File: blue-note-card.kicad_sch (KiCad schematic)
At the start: 27 parts, among them J15 N_GR1, J3 MDT420E01001, J7 SF72S006VBAR2500, J9 N_GR2

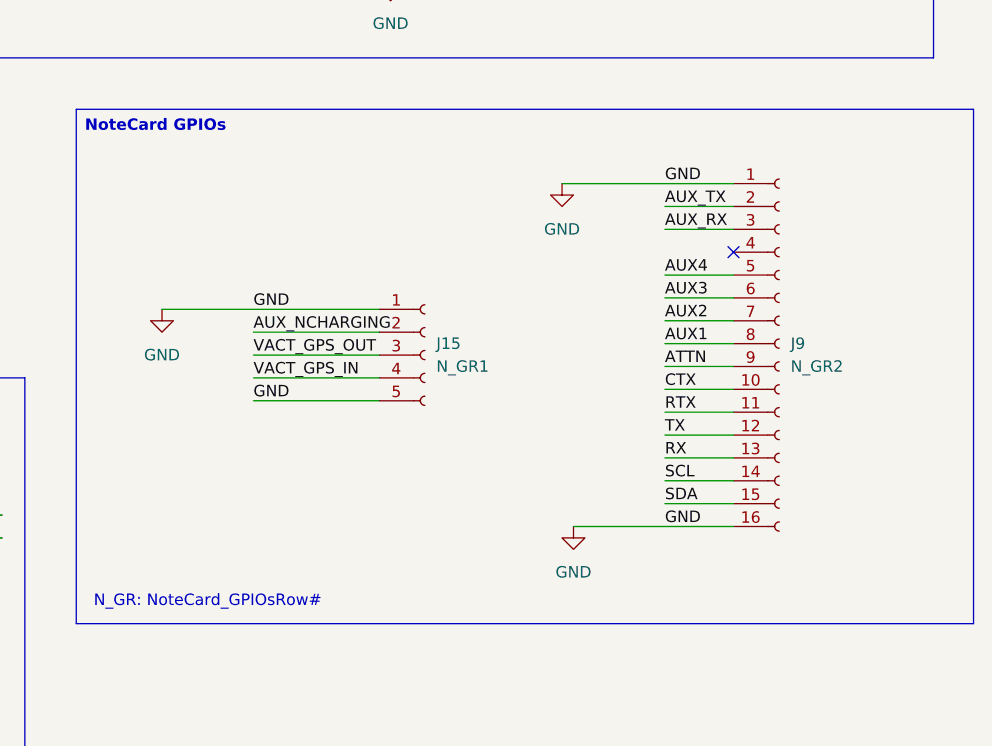
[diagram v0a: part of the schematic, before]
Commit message: Layout parts
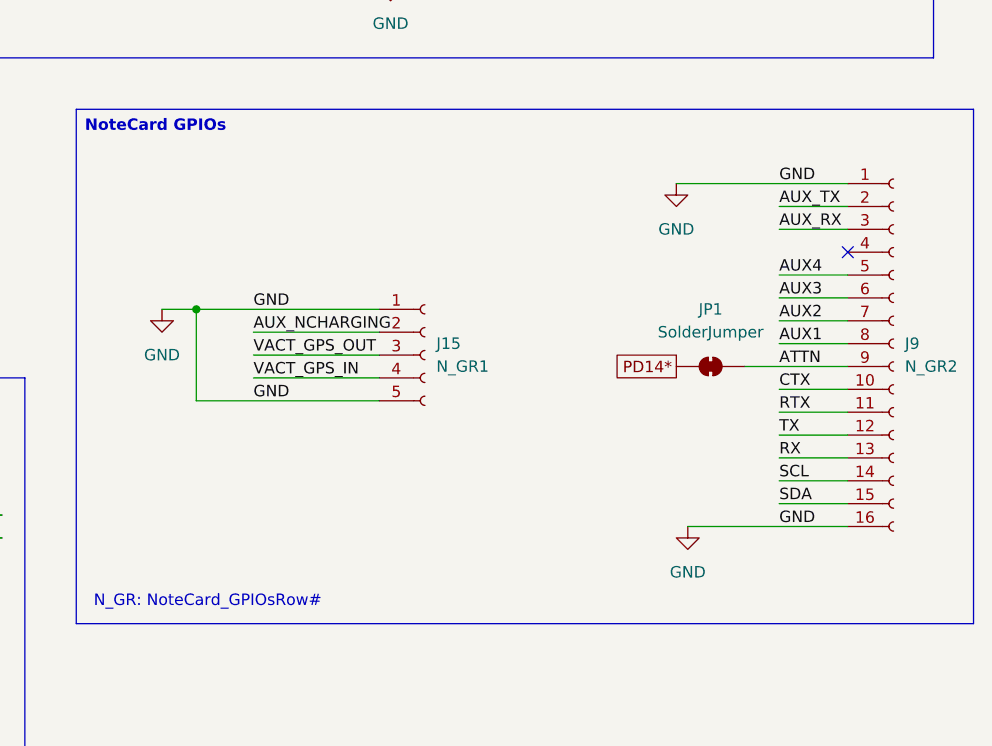
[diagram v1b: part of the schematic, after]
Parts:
- added JP1: SolderJumper, Jumper:SolderJumper-2_P1.3mm_Bridged_RoundedPad1.0x1.5mm, symbol Jumper:SolderJumper_2_Bridged
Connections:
- net ATTN: now also JP1.2 (B)
- new net PD14*: JP1.1 (A)
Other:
- moved on the sheet: J9

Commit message: Layout
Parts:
- removed JP1: SolderJumper, Jumper:SolderJumper-2_P1.3mm_Bridged_RoundedPad1.0x1.5mm, symbol Jumper:SolderJumper_2_Bridged
- added JP1: SolderJumper_2_Open, Jumper:SolderJumper-2_P1.3mm_Open_RoundedPad1.0x1.5mm, symbol Jumper:SolderJumper_2_Open
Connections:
- net +3.3V Buck: now also J3.2, J3.4
- net ATTN: now also J9.6 (Pin_6); no longer J9.9 (Pin_9)
- net AUX1: now also J9.10 (Pin_10); no longer J9.8 (Pin_8)
- net AUX2: now also J9.9 (Pin_9); no longer J9.7 (Pin_7)
- net AUX3: now also J9.8 (Pin_8); no longer J9.6 (Pin_6)
- net AUX4: now also J9.7 (Pin_7); no longer J9.5 (Pin_5)
- net AUX_NCHARGING: now also J9.13 (Pin_13); no longer J15.2 (Pin_2)
- net AUX_RX: now also J9.5 (Pin_5); no longer J9.3 (Pin_3)
- net AUX_TX: now also J9.4 (Pin_4); no longer J9.2 (Pin_2)
- net CTX: now also J15.2 (Pin_2); no longer J9.10 (Pin_10)
- net GND: no longer J3.2, J3.4
- net RTX: now also J15.3 (Pin_3); no longer J9.11 (Pin_11)
- net RX: now also J9.3 (Pin_3); no longer J9.13 (Pin_13)
- net SCL: now also J9.12 (Pin_12); no longer J9.14 (Pin_14)
- net SDA: now also J9.11 (Pin_11); no longer J9.15 (Pin_15)
- net TX: now also J9.2 (Pin_2); no longer J9.12 (Pin_12)
- net VACT_GPS_IN: now also J9.14 (Pin_14), JP1.1 (A); no longer J15.4 (Pin_4)
- net VACT_GPS_OUT: now also J9.15 (Pin_15), JP1.2 (B); no longer J15.3 (Pin_3)

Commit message: Fixed DRC errors
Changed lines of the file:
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@@
-	(wire
-		(pts
-			(xy 259.08 116.84) (xy 266.7 116.84)
-		)
-		(stroke
-			(width 0)
-			(type default)
-		)
-	)
 	(wire
 		(pts

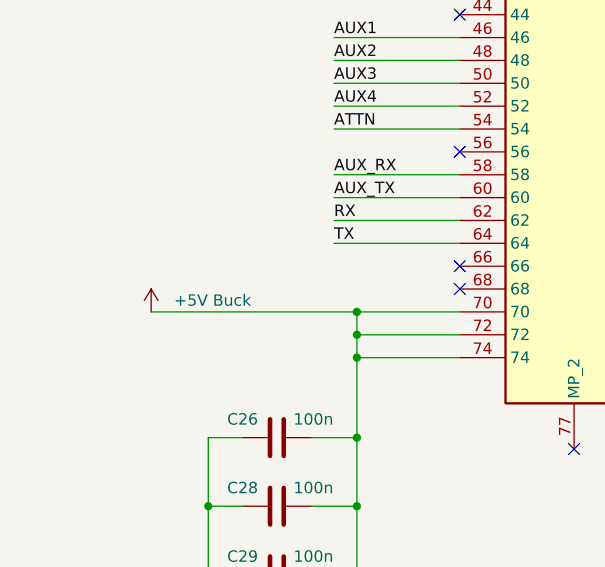
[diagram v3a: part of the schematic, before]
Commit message: Added ORing VBUS
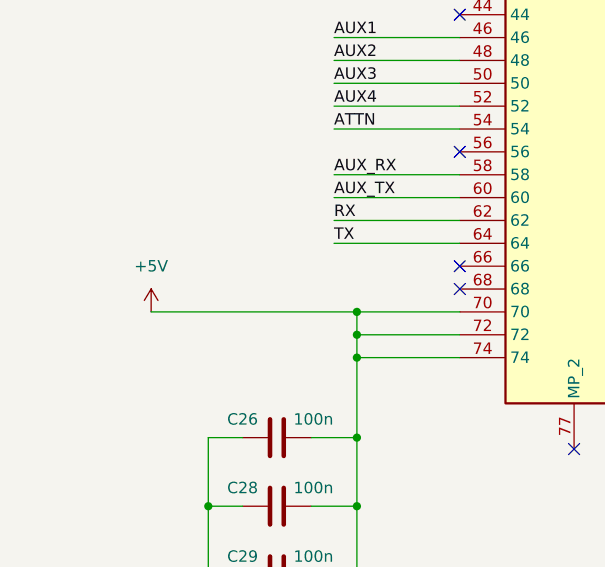
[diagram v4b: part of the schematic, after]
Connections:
- net +5V Buck renamed +5V
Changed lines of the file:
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@@
 			)
 		)
-		(property "Value" "+5V Buck"
-			(at 22.86 121.9199 0)
+		(property "Value" "+5V"
+			(at 20.32 118.11 0)
 			(effects
 				(font
 					(size 1.27 1.27)
 				)
-				(justify left)
 			)
 		)

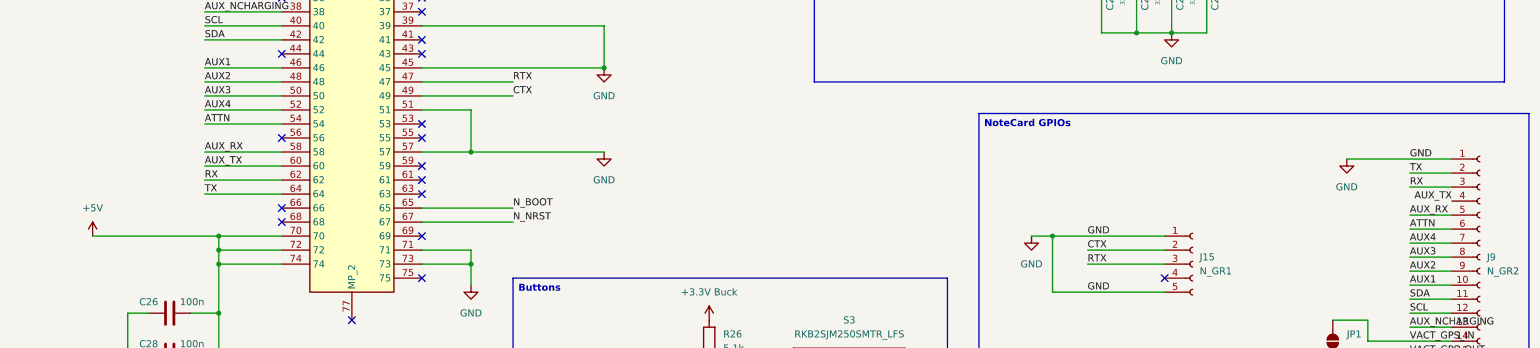
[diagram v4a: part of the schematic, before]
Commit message: Added LED indicators, USER LEDs, extended layout, fixed footprints
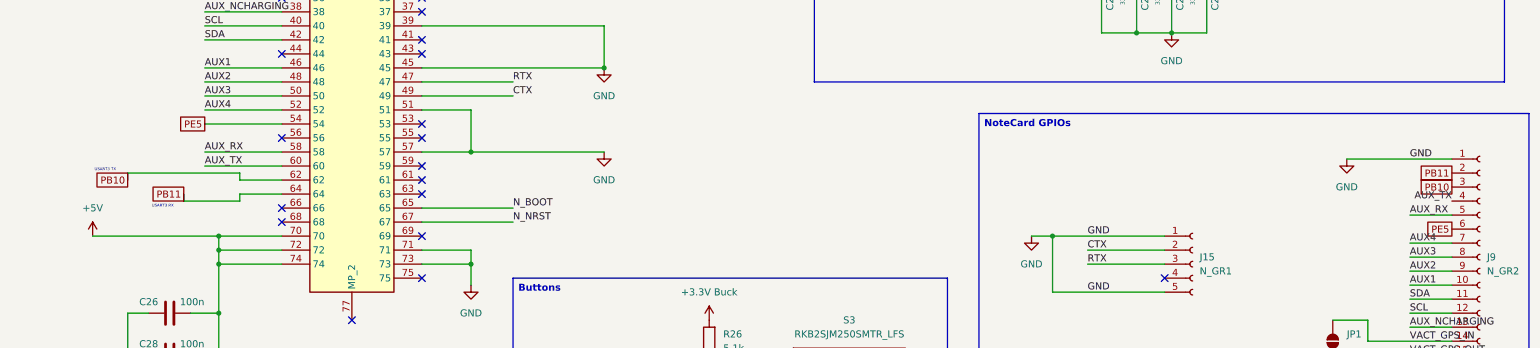
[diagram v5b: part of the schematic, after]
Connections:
- net ATTN renamed PE5
- net RX renamed PB10
- net TX renamed PB11
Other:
- note added: "USART3 RX"
- note added: "USART3 TX"
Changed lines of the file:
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@@
+		)
+	)
+	(text "USART3 RX"
+		(exclude_from_sim no)
+		(at 33.02 117.856 0)
+		(effects
+			(font
+				(size 0.508 0.508)
+			)
+		)
+	)
+	(text "USART3 TX"
+		(exclude_from_sim no)
+		(at 22.606 111.252 0)
+		(effects
+			(font
+				(size 0.508 0.508)
+			)
 		)
 	)
@@
 	(wire
 		(pts
+			(xy 46.99 115.57) (xy 46.99 116.84)
+		)
+		(stroke
+			(width 0)
+			(type default)
+		)
+	)
+	(wire
+		(pts
 			(xy 264.16 33.02) (xy 264.16 35.56)
 		)
@@
 	(wire
 		(pts
+			(xy 46.99 111.76) (xy 26.67 111.76)
+		)
+		(stroke
+			(width 0)
+			(type default)
+		)
+	)
+	(wire
+		(pts
 			(xy 30.48 137.16) (xy 26.67 137.16)
 		)
@@
 	(wire
 		(pts
+			(xy 36.83 116.84) (xy 36.83 115.57)
+		)
+		(stroke
+			(width 0)
+			(type default)
+		)
+	)
+	(wire
+		(pts
 			(xy 19.05 67.31) (xy 54.61 67.31)
 		)
@@
 	(wire
 		(pts
-			(xy 259.08 111.76) (xy 266.7 111.76)
-		)
-		(stroke
-			(width 0)
-			(type default)
-		)
-	)
-	(wire
-		(pts
 			(xy 167.64 66.04) (xy 160.02 66.04)
 		)
@@
 	(wire
 		(pts
-			(xy 54.61 115.57) (xy 40.64 115.57)
+			(xy 54.61 115.57) (xy 46.99 115.57)
 		)
 		(stroke
@@
 	(wire
 		(pts
+			(xy 46.99 113.03) (xy 46.99 111.76)
+		)
+		(stroke
+			(width 0)
+			(type default)
+		)
+	)
+	(wire
+		(pts
 			(xy 80.01 107.95) (xy 88.9 107.95)
 		)
@@
 	(wire
 		(pts
-			(xy 259.08 114.3) (xy 266.7 114.3)
-		)
-		(stroke
-			(width 0)
-			(type default)
-		)
-	)
-	(wire
-		(pts
 			(xy 264.16 40.64) (xy 264.16 43.18)
 		)
@@
 	(wire
 		(pts
+			(xy 26.67 111.76) (xy 26.67 113.03)
+		)
+		(stroke
+			(width 0)
+			(type default)
+		)
+	)
+	(wire
+		(pts
 			(xy 80.01 97.79) (xy 96.52 97.79)
 		)
@@
 	(wire
 		(pts
-			(xy 259.08 121.92) (xy 266.7 121.92)
-		)
-		(stroke
-			(width 0)
-			(type default)
-		)
-	)
-	(wire
-		(pts
 			(xy 196.85 45.72) (xy 209.55 45.72)
 		)
@@
 	(wire
 		(pts
-			(xy 54.61 113.03) (xy 40.64 113.03)
+			(xy 54.61 113.03) (xy 46.99 113.03)
 		)
 		(stroke
@@
 		(pts
 			(xy 251.46 144.78) (xy 266.7 144.78)
+		)
+		(stroke
+			(width 0)
+			(type default)
+		)
+	)
+	(wire
+		(pts
+			(xy 46.99 116.84) (xy 36.83 116.84)
 		)
 		(stroke
@@
 		)
 	)
-	(label "TX"
-		(at 259.08 111.76 0)
-		(effects
-			(font
-				(size 1.27 1.27)
-				(thickness 0.1588)
-			)
-			(justify left bottom)
-		)
-	)
 	(label "GND"
 		(at 200.66 123.19 0)
@@
 		)
 	)
-	(label "RX"
-		(at 40.64 113.03 0)
-		(effects
-			(font
-				(size 1.27 1.27)
-			)
-			(justify left bottom)
-		)
-	)
 	(label "RTX"
 		(at 96.52 95.25 0)
@@
 		)
 	)
-	(label "TX"
-		(at 40.64 115.57 0)
-		(effects
-			(font
-				(size 1.27 1.27)
-			)
-			(justify left bottom)
-		)
-	)
 	(label "SCL"
 		(at 259.08 137.16 0)
@@
 		)
 	)
-	(label "RX"
-		(at 259.08 114.3 0)
-		(effects
-			(font
-				(size 1.27 1.27)
-				(thickness 0.1588)
-			)
-			(justify left bottom)
-		)
-	)
-	(label "ATTN"
-		(at 40.64 102.87 0)
-		(effects
-			(font
-				(size 1.27 1.27)
-			)
-			(justify left bottom)
-		)
-	)
 	(label "SIM_RST"
 		(at 173.99 35.56 0)
@@
 		)
 	)
-	(label "ATTN"
-		(at 259.08 121.92 0)
-		(effects
-			(font
-				(size 1.27 1.27)
-			)
-			(justify left bottom)
-		)
-	)
 	(label "SIM_RST"
 		(at 40.64 57.15 0)
@@
 		)
 	)
+	(global_label "PE5"
+		(shape passive)
+		(at 266.7 121.92 180)
+		(fields_autoplaced yes)
+		(effects
+			(font
+				(size 1.27 1.27)
+			)
+			(justify right)
+		)
+		(property "Intersheetrefs" "${INTERSHEET_REFS}"
+			(at 261.1976 121.92 0)
+			(effects
+				(font
+					(size 1.27 1.27)
+				)
+				(justify right)
+				(hide yes)
+			)
+		)
+	)
+	(global_label "PB11"
+		(shape passive)
+		(at 36.83 115.57 180)
+		(fields_autoplaced yes)
+		(effects
+			(font
+				(size 1.27 1.27)
+			)
+			(justify right)
+		)
+		(property "Intersheetrefs" "${INTERSHEET_REFS}"
+			(at 29.9971 115.57 0)
+			(effects
+				(font
+					(size 1.27 1.27)
+				)
+				(justify right)
+				(hide yes)
+			)
+		)
+	)
+	(global_label "PB10"
+		(shape passive)
+		(at 26.67 113.03 180)
+		(fields_autoplaced yes)
+		(effects
+			(font
+				(size 1.27 1.27)
+			)
+			(justify right)
+		)
+		(property "Intersheetrefs" "${INTERSHEET_REFS}"
+			(at 19.8371 113.03 0)
+			(effects
+				(font
+					(size 1.27 1.27)
+				)
+				(justify right)
+				(hide yes)
+			)
+		)
+	)
+	(global_label "PE5"
+		(shape passive)
+		(at 40.64 102.87 180)
+		(fields_autoplaced yes)
+		(effects
+			(font
+				(size 1.27 1.27)
+			)
+			(justify right)
+		)
+		(property "Intersheetrefs" "${INTERSHEET_REFS}"
+			(at 35.1376 102.87 0)
+			(effects
+				(font
+					(size 1.27 1.27)
+				)
+				(justify right)
+				(hide yes)
+			)
+		)
+	)
+	(global_label "PB11"
+		(shape passive)
+		(at 266.7 111.76 180)
+		(fields_autoplaced yes)
+		(effects
+			(font
+				(size 1.27 1.27)
+			)
+			(justify right)
+		)
+		(property "Intersheetrefs" "${INTERSHEET_REFS}"
+			(at 259.8671 111.76 0)
+			(effects
+				(font
+					(size 1.27 1.27)
+				)
+				(justify right)
+				(hide yes)
+			)
+		)
+	)
+	(global_label "PB10"
+		(shape passive)
+		(at 266.7 114.3 180)
+		(fields_autoplaced yes)
+		(effects
+			(font
+				(size 1.27 1.27)
+			)
+			(justify right)
+		)
+		(property "Intersheetrefs" "${INTERSHEET_REFS}"
+			(at 259.8671 114.3 0)
+			(effects
+				(font
+					(size 1.27 1.27)
+				)
+				(justify right)
+				(hide yes)
+			)
+		)
+	)

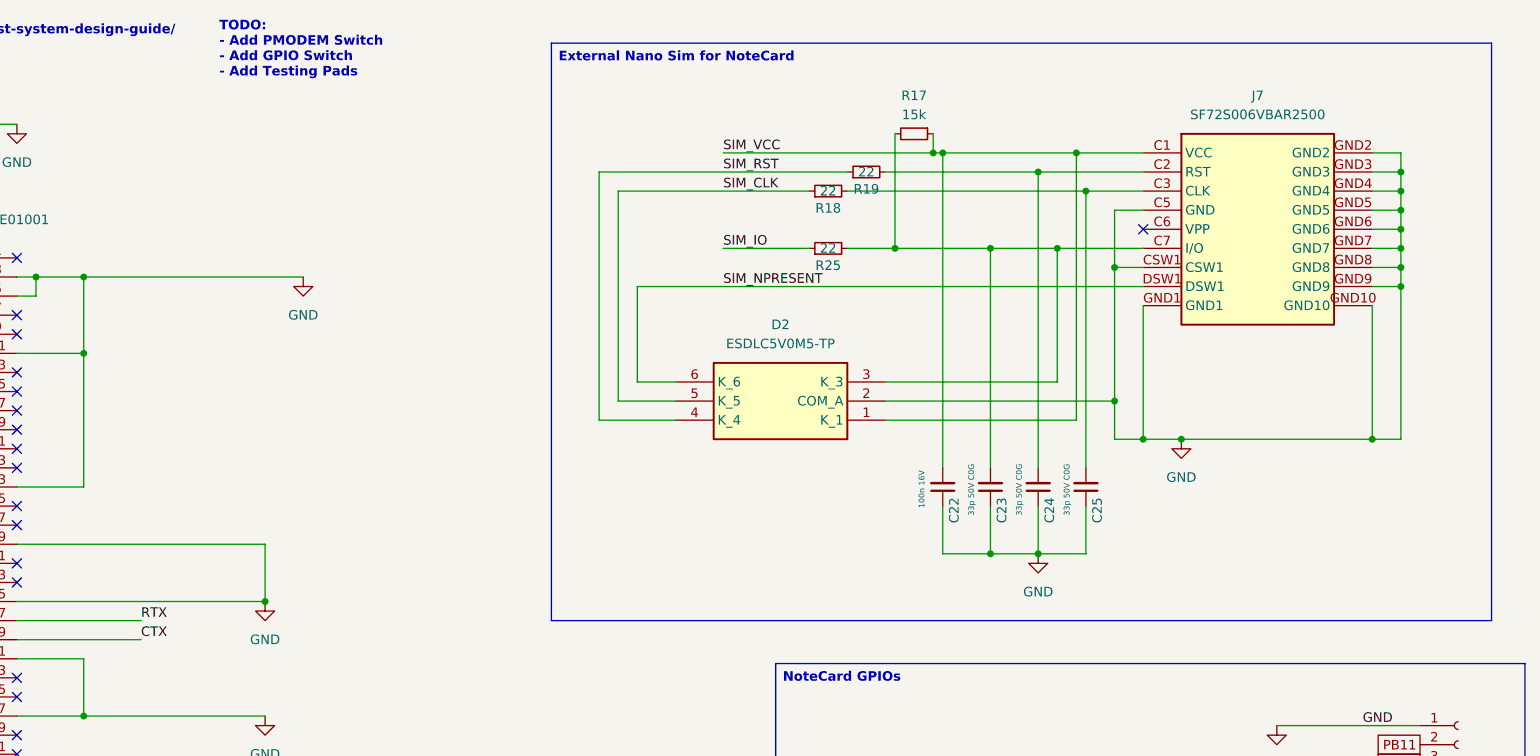
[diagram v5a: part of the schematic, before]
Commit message: Relayout NanoSim component
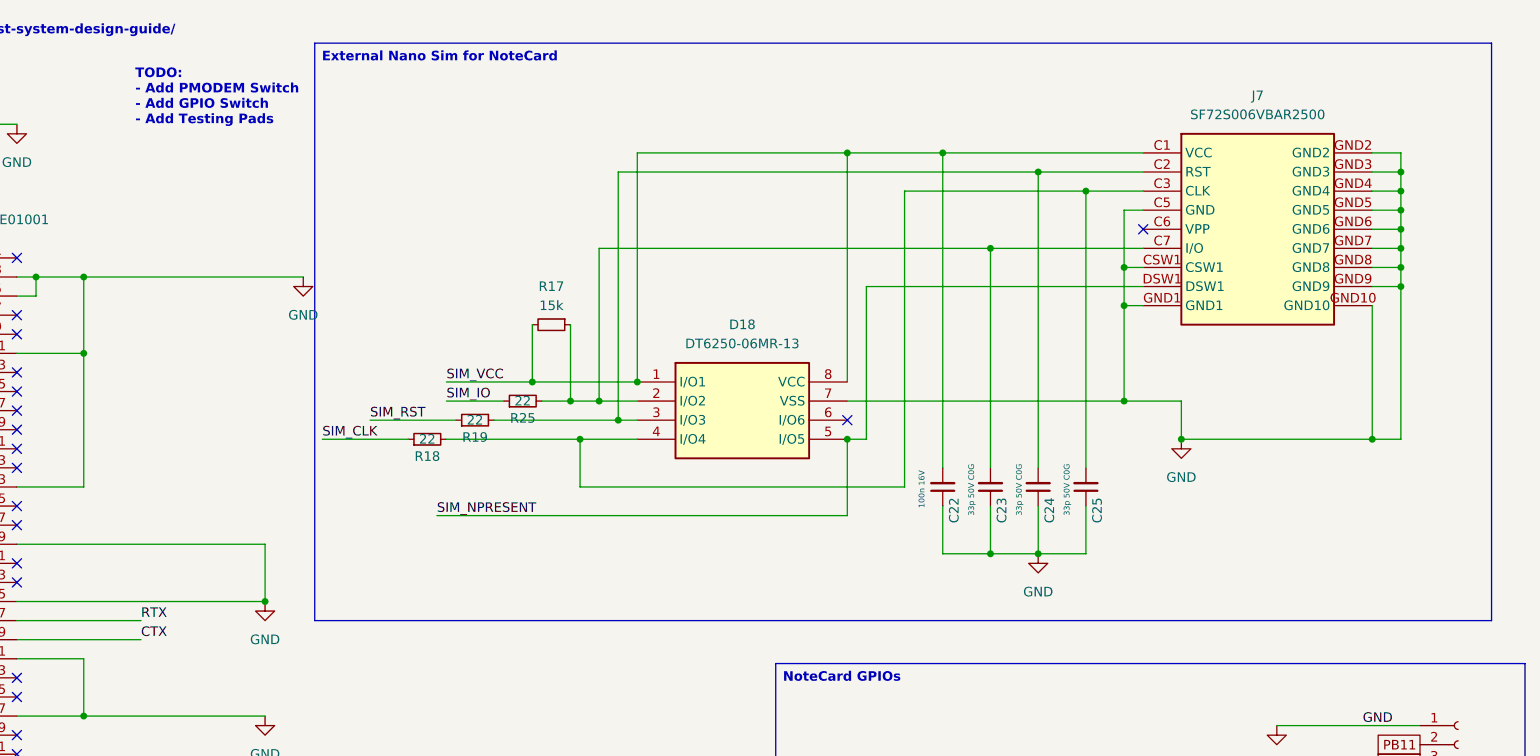
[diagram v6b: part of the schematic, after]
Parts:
- removed D2: ESDLC5V0M5-TP, SamacSys_Parts:SOTFL50P160X60-6N, symbol SamacSys_Parts:ESDLC5V0M5-TP
- added D18: DT6250-06MR-13, SamacSys_Parts:SOP65P490X110-8N, symbol SamacSys_Parts:DT6250-06MR-13
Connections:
- net GND: now also D18.7 (VSS)
- net SIM_NPRESENT: now also D18.5 (I/O5)
- net SIM_VCC: now also R17.2, D18.1 (I/O1), D18.8 (VCC); no longer R17.1
- net at C25.2, J7.C3 (CLK), R18.2: now also D18.4 (I/O4)
- net at C23.2, J7.C7 (I/O), R25.2: now also R17.1, D18.2 (I/O2); no longer R17.2
- net at C24.2, J7.C2 (RST), R19.2: now also D18.3 (I/O3)
- no-connect marks 31 -> 32
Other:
- moved on the sheet: R17, R18, R19, R25

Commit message: Added changes
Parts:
- removed J15: N_GR1, Connector_PinSocket_2.00mm:PinSocket_1x05_P2.00mm_Vertical, symbol Connector:Conn_01x05_Socket
- removed J9: N_GR2, Connector_PinSocket_2.00mm:PinSocket_1x16_P2.00mm_Vertical, symbol Connector:Conn_01x16_Socket
- added J17: N_GR1, Connector_PinSocket_2.00mm:PinSocket_1x20_P2.00mm_Vertical, symbol Connector:Conn_01x20_Socket
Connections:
- net AUX1: now also J17.10 (Pin_10)
- net AUX2: now also J17.9 (Pin_9)
- net AUX3: now also J17.8 (Pin_8)
- net AUX4: now also J17.7 (Pin_7)
- net AUX_NCHARGING: now also J17.13 (Pin_13)
- net AUX_RX: now also J17.5 (Pin_5)
- net AUX_TX: now also J17.4 (Pin_4)
- net CTX: now also J17.16 (Pin_16)
- net GND: now also J17.1 (Pin_1), J17.18 (Pin_18), J17.19 (Pin_19), J17.20 (Pin_20)
- net PB10: now also J17.3 (Pin_3)
- net PB11: now also J17.2 (Pin_2)
- net PE5: now also J17.6 (Pin_6)
- net RTX: now also J17.17 (Pin_17)
- net SCL: now also J17.12 (Pin_12)
- net SDA: now also J17.11 (Pin_11)
- net VACT_GPS_IN: now also J17.14 (Pin_14)
- net VACT_GPS_OUT: now also J17.15 (Pin_15)
- no-connect marks 32 -> 31

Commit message: Fixed things
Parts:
- removed C54, C55: 100n, Capacitor_SMD:C_0603_1608Metric_Pad1.08x0.95mm_HandSolder, symbol Device:C
- removed R26, R27: 5.1k, Resistor_SMD:R_0603_1608Metric_Pad0.98x0.95mm_HandSolder, symbol Device:R
- removed S4: RKB2SJM250SMTR_LFS, SamacSys_Parts:RKB2SJM250SMTRLFS, symbol SamacSys_Parts:RKB2SJM250SMTR_LFS
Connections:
- net +3.3V Buck renamed +3.3V NOTE
- net +5V renamed +5V NOTE
- net N_BOOT: no longer names the net of J3.65
- net PB10 renamed PB10_PIN_HEADER
- no-connect marks 31 -> 32
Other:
- note added: "BlueNoteCard internal circuitry already has pull-down resistor. Do not add pull-down resistor here"
- moved on the sheet: S3
